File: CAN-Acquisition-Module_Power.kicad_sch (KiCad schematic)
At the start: 37 parts, among them J1 Conn_01x04, J2 Conn_01x02, Q1 SI2318A, U1 TL431DBZ, U2 S-8581AA

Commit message: Finished power outputs
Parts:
- L2: value 470 uF -> 470 uH
- U1: value TL431DBZ -> AZ431LAN
- renumbered C11 to C10, C12 to C11, C13 to C12, C14 to C13, C4 to C3, C5 to C4, C6 to C5, C7 to C6, C8 to C7, C9 to C8, C10 to C9
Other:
- note added: "1.24V"
- note added: "20ppm/°C or better"

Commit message: Only CAN transceiver left
SPi flash should be added too
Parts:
- added NT1: NetTie_2, CAN-Acquisition-Module:Net_Tie_small, symbol Device:NetTie_2
- C6: footprint Capacitor_THT:CP_Radial_D10.0mm_P5.00mm -> CAN-Acquisition-Module:CP_Radial_D10.0mm_P5.00mm_Horizontal
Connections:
- net at C6.1, C7.1, C8.1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: now also NT1.1; no longer U2.1 (VIN), U2.3 (EN)
- new net: NT1.2, U2.1 (VIN), U2.3 (EN)
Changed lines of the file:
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@@
     (stroke (width 0) (type default) (color 0 0 0 0))
   )
-  (wire (pts (xy 177.8 95.25) (xy 170.18 95.25))
+  (wire (pts (xy 177.8 95.25) (xy 176.53 95.25))
     (stroke (width 0) (type default) (color 0 0 0 0))
   )
@@
   )
   (wire (pts (xy 203.2 100.33) (xy 207.01 100.33))
+    (stroke (width 0) (type default) (color 0 0 0 0))
+  )
+  (wire (pts (xy 171.45 95.25) (xy 170.18 95.25))
     (stroke (width 0) (type default) (color 0 0 0 0))
   )
@@
       (effects (font (size 1.27 1.27)) (justify left))
     )
-    (property "Footprint" "Capacitor_THT:CP_Radial_D10.0mm_P5.00mm" (id 2) (at 140.97 119.38 90)
+    (property "Footprint" "CAN-Acquisition-Module:CP_Radial_D10.0mm_P5.00mm_Horizontal" (id 2) (at 140.97 119.38 90)
       (effects (font (size 1.27 1.27)) hide)
     )
@@
       (effects (font (size 1.27 1.27)) hide)
     )
+    (pin "1")
+    (pin "2")
+  )
+  (symbol (lib_id "Device:NetTie_2") (at 173.99 95.25 0) (unit 1)
+    (in_bom yes) (on_board yes) (fields_autoplaced)
+    (property "Reference" "NT1" (id 0) (at 173.99 91.5502 0))
+    (property "Value" "NetTie_2" (id 1) (at 173.99 94.0871 0))
+    (property "Footprint" "CAN-Acquisition-Module:Net_Tie_small" (id 2) (at 173.99 95.25 0)
+      (effects (font (size 1.27 1.27)) hide)
+    )
+    (property "Datasheet" "~" (id 3) (at 173.99 95.25 0)
+      (effects (font (size 1.27 1.27)) hide)
+    )

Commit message: forgor to save
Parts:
- added C13: 10 uF, Capacitor_SMD:C_0805_2012Metric, symbol Device:C_Small
- renumbered C13 to C14
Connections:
- net +3V3: now also C13.1
- net GND: now also C13.2
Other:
- moved on the sheet: C14

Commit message: Rev. A1 release
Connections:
- net at NT1.2, U2.1 (VIN), U2.3 (EN): now also C7.1, C8.1
- net at C6.1, L2.2, NT1.1: no longer C7.1, C8.1
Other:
- note added: "50V"
- note added: "50V rating"
- note added: "}"
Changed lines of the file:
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@@
-    (stroke (width 0) (type default) (color 0 0 0 0))
-  )
-  (wire (pts (xy 177.8 95.25) (xy 176.53 95.25))
     (stroke (width 0) (type default) (color 0 0 0 0))
   )
@@
     (stroke (width 0) (type default) (color 0 0 0 0))
   )
+  (wire (pts (xy 153.67 95.25) (xy 157.48 95.25))
+    (stroke (width 0) (type default) (color 0 0 0 0))
+  )
   (wire (pts (xy 157.48 95.25) (xy 157.48 100.33))
     (stroke (width 0) (type default) (color 0 0 0 0))
@@
     (stroke (width 0) (type default) (color 0 0 0 0))
   )
-  (wire (pts (xy 171.45 95.25) (xy 170.18 95.25))
+  (wire (pts (xy 170.18 95.25) (xy 177.8 95.25))
     (stroke (width 0) (type default) (color 0 0 0 0))
   )
@@
     (stroke (width 0) (type default) (color 0 0 0 0))
   )
-  (wire (pts (xy 144.78 95.25) (xy 157.48 95.25))
+  (wire (pts (xy 144.78 95.25) (xy 148.59 95.25))
     (stroke (width 0) (type default) (color 0 0 0 0))
   )
@@
     (stroke (width 0) (type default) (color 0 0 0 0))
   )
-  (text "5 to 24V" (at 152.4 95.25 0)
+  (text "}" (at 170.18 95.25 90)
+    (effects (font (size 20 20)) (justify left bottom))
+  )
+  (text "50V" (at 114.3 106.68 0)
+    (effects (font (size 1.27 1.27)) (justify left bottom))
+  )
+  (text "5 to 24V" (at 153.67 95.25 0)
     (effects (font (size 1.27 1.27)) (justify left bottom))
   )
@@
   )
   (text "1.24V" (at 60.96 170.18 0)
+    (effects (font (size 1.27 1.27)) (justify left bottom))
+  )
+  (text "50V rating" (at 153.67 85.09 0)
     (effects (font (size 1.27 1.27)) (justify left bottom))
   )
@@
       (effects (font (size 1.27 1.27)) hide)
     )
-    (property "P/N" "GRM31CR71H475KA12L" (id 7) (at 153.67 118.11 90))
+    (property "P/N" "GRM31CR71H475KA12L" (id 7) (at 153.67 115.57 90))
     (property "Rated Voltage" "50V" (id 8) (at 157.48 102.87 0)
       (effects (font (size 1.27 1.27)) hide)
@@
     (pin "2")
   )
-  (symbol (lib_id "Device:NetTie_2") (at 173.99 95.25 0) (unit 1)
-    (in_bom yes) (on_board yes) (fields_autoplaced)
-    (property "Reference" "NT1" (id 0) (at 173.99 91.5502 0))
-    (property "Value" "NetTie_2" (id 1) (at 173.99 94.0871 0))
-    (property "Footprint" "CAN-Acquisition-Module:Net_Tie_small" (id 2) (at 173.99 95.25 0)
-      (effects (font (size 1.27 1.27)) hide)
-    )
-    (property "Datasheet" "~" (id 3) (at 173.99 95.25 0)
-      (effects (font (size 1.27 1.27)) hide)
-    )
+  (symbol (lib_id "Device:NetTie_2") (at 151.13 95.25 0) (unit 1)
+    (in_bom yes) (on_board yes) (fields_autoplaced)
+    (property "Reference" "NT1" (id 0) (at 151.13 91.5502 0)
+      (effects (font (size 1.27 1.27)) hide)
+    )
+    (property "Value" "NetTie_2" (id 1) (at 151.13 94.0871 0)
+      (effects (font (size 1.27 1.27)) hide)
+    )
+    (property "Footprint" "CAN-Acquisition-Module:Net_Tie_small" (id 2) (at 151.13 95.25 0)
+      (effects (font (size 1.27 1.27)) hide)
+    )
+    (property "Datasheet" "~" (id 3) (at 151.13 95.25 0)
+      (effects (font (size 1.27 1.27)) hide)
+    )

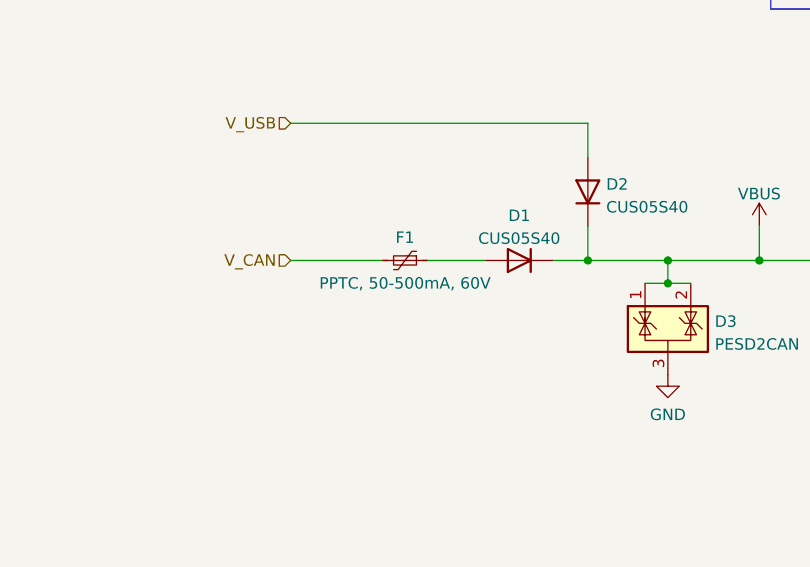
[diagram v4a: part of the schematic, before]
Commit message: Added as-ordered P/Ns and regenerated Gerbers
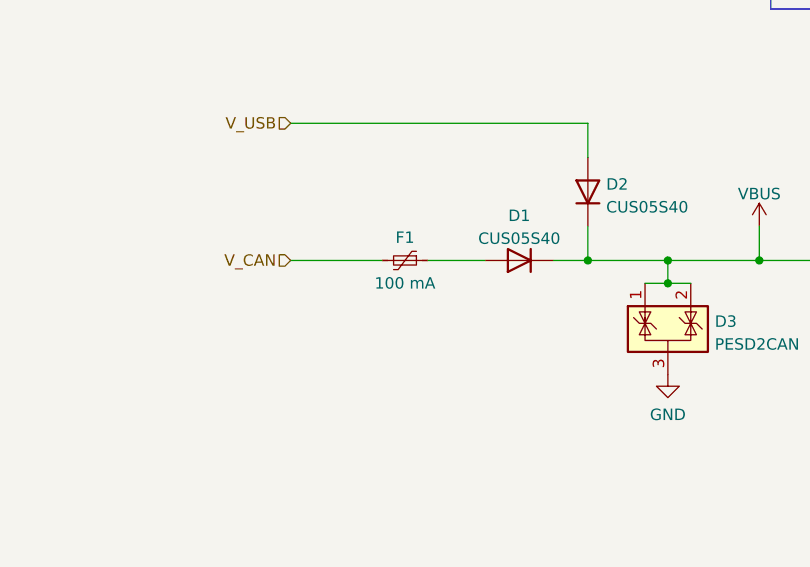
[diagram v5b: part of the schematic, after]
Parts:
- C11: Mfr. (none) -> Kemet; P/N (none) -> C0603C330J1GACAUTO
- D1, D2, D6: P/N (none) -> CUS05S40,H3F
- D3: Mfr. (none) -> Comchip Technology; P/N (none) -> CPDT-24V
- D4, D5: Mfr. (none) -> Diodes Incorporated; P/N (none) -> D1213A-01SO-7
- F1: value PPTC, 50-500mA, 60V -> 100 mA
- L1: Mfr. (none) -> Eaton; P/N (none) -> MFBM1V1608-300-R
- L2: Mfr. (none) -> Murata Electronics
- Q1: Mfr. (none) -> Micro Commercial Co.; P/N (none) -> SI2318A-TP
- R1: Mfr. (none) -> Stackpole; P/N (none) -> RNCP0805FTD100R
- R2: Mfr. (none) -> Panasonic; P/N (none) -> ERJ-PB3B6801V
- R3, R9: Mfr. (none) -> KOA Speer; P/N (none) -> RN73R1JTTD1502B25
- R5, R6, R7: Mfr. (none) -> Stackpole; P/N (none) -> RMCF0603FT10K0
- R8: Mfr. (none) -> TE Connectivity; P/N (none) -> CRGCQ0603F47K
- U1: Mfr. (none) -> Diodes Incorporated; P/N (none) -> AZ431LANTR-G1
- U2: Mfr. (none) -> Ablic; P/N (none) -> S-8581AA-A8T1U7
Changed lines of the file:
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@@
       (effects (font (size 1.27 1.27) italic) hide)
     )
+    (property "Mfr." "Diodes Incorporated" (id 4) (at 67.31 170.18 0)
+      (effects (font (size 1.27 1.27)) hide)
+    )
+    (property "P/N" "AZ431LANTR-G1" (id 5) (at 67.31 170.18 0)
+      (effects (font (size 1.27 1.27)) hide)
+    )
     (pin "1")
     (pin "2")
@@
       (effects (font (size 1.27 1.27)) hide)
     )
+    (property "Mfr." "Panasonic" (id 4) (at 57.15 166.37 0)
+      (effects (font (size 1.27 1.27)) hide)
+    )
+    (property "P/N" "ERJ-PB3B6801V" (id 5) (at 57.15 166.37 0)
+      (effects (font (size 1.27 1.27)) hide)
+    )
     (pin "1")
     (pin "2")
@@
     )
     (property "Datasheet" "~" (id 3) (at 57.15 173.99 0)
+      (effects (font (size 1.27 1.27)) hide)
+    )
+    (property "Mfr." "KOA Speer" (id 4) (at 57.15 173.99 0)
+      (effects (font (size 1.27 1.27)) hide)
+    )
+    (property "P/N" "RN73R1JTTD1502B25" (id 5) (at 57.15 173.99 0)
       (effects (font (size 1.27 1.27)) hide)
     )
@@
       (effects (font (size 1.27 1.27)) hide)
     )
+    (property "Mfr." "Stackpole" (id 4) (at 49.53 161.29 0)
+      (effects (font (size 1.27 1.27)) hide)
+    )
+    (property "P/N" "RNCP0805FTD100R" (id 5) (at 49.53 161.29 0)
+      (effects (font (size 1.27 1.27)) hide)
+    )
     (pin "1")
     (pin "2")
@@
       (effects (font (size 1.27 1.27)) hide)
     )
+    (property "Mfr." "Eaton" (id 4) (at 39.37 161.29 0)
+      (effects (font (size 1.27 1.27)) hide)
+    )
+    (property "P/N" "MFBM1V1608-300-R" (id 5) (at 39.37 161.29 0)
+      (effects (font (size 1.27 1.27)) hide)
+    )
     (pin "1")
     (pin "2")
@@
       (effects (font (size 1.27 1.27)) hide)
     )
+    (property "P/N" "CUS05S40,H3F" (id 5) (at 238.76 34.29 0)
+      (effects (font (size 1.27 1.27)) hide)
+    )
     (pin "1")
     (pin "2")
@@
     )
     (property "Datasheet" "https://assets.nexperia.com/documents/data-sheet/PESD2CAN.pdf" (id 3) (at 94.615 99.695 0)
+      (effects (font (size 1.27 1.27)) hide)
+    )
+    (property "Mfr." "Comchip Technology" (id 4) (at 91.44 102.87 0)
+      (effects (font (size 1.27 1.27)) hide)
+    )
+    (property "P/N" "CPDT-24V" (id 5) (at 91.44 102.87 0)
       (effects (font (size 1.27 1.27)) hide)
     )
@@
     )
     (property "Datasheet" "https://www.ablic.com/en/doc/datasheet/switching_regulator/S8580AA_8580AB_8581AA_8581AB_E.pdf" (id 3) (at 201.93 120.65 0)
+      (effects (font (size 1.27 1.27)) hide)
+    )
+    (property "Mfr." "Ablic" (id 4) (at 187.96 92.71 0)
+      (effects (font (size 1.27 1.27)) hide)
+    )
+    (property "P/N" "S-8581AA-A8T1U7" (id 5) (at 187.96 92.71 0)
       (effects (font (size 1.27 1.27)) hide)
     )
@@
       (effects (font (size 1.27 1.27)) hide)
     )
+    (property "Mfr." "Stackpole" (id 4) (at 173.99 44.45 0)
+      (effects (font (size 1.27 1.27)) hide)
+    )
+    (property "P/N" "RMCF0603FT10K0" (id 5) (at 173.99 44.45 0)
+      (effects (font (size 1.27 1.27)) hide)
+    )
     (pin "1")
     (pin "2")
@@
       (effects (font (size 1.27 1.27)) hide)
     )
+    (property "Mfr." "Murata Electronics" (id 5) (at 124.46 95.25 0)
+      (effects (font (size 1.27 1.27)) hide)
+    )
     (pin "1")
     (pin "2")
@@
       (effects (font (size 1.27 1.27)) hide)
     )
+    (property "Mfr." "Diodes Incorporated" (id 4) (at 168.91 26.67 0)
+      (effects (font (size 1.27 1.27)) hide)
+    )
+    (property "P/N" "D1213A-01SO-7" (id 5) (at 168.91 26.67 0)
+      (effects (font (size 1.27 1.27)) hide)
+    )
     (pin "1")
     (pin "2")
@@
       (effects (font (size 1.27 1.27)) hide)
     )
+    (property "Mfr." "Stackpole" (id 4) (at 227.33 53.34 0)
+      (effects (font (size 1.27 1.27)) hide)
+    )
+    (property "P/N" "RMCF0603FT10K0" (id 5) (at 227.33 53.34 0)
+      (effects (font (size 1.27 1.27)) hide)
+    )
     (pin "1")
     (pin "2")
@@
       (effects (font (size 1.27 1.27)) hide)
     )
+    (property "P/N" "CUS05S40,H3F" (id 5) (at 82.55 87.63 0)
+      (effects (font (size 1.27 1.27)) hide)
+    )
     (pin "1")
     (pin "2")
@@
       (effects (font (size 1.27 1.27)) hide)
     )
+    (property "Mfr." "Diodes Incorporated" (id 4) (at 146.05 26.67 0)
+      (effects (font (size 1.27 1.27)) hide)
+    )
+    (property "P/N" "D1213A-01SO-7" (id 5) (at 146.05 26.67 0)
+      (effects (font (size 1.27 1.27)) hide)
+    )
     (pin "1")
     (pin "2")
@@
       (effects (font (size 1.27 1.27)) hide)
     )
+    (property "Mfr." "KOA Speer" (id 4) (at 232.41 105.41 0)
+      (effects (font (size 1.27 1.27)) hide)
+    )
+    (property "P/N" "RN73R1JTTD1502B25" (id 5) (at 232.41 105.41 0)
+      (effects (font (size 1.27 1.27)) hide)
+    )
     (pin "1")
     (pin "2")
@@
     )
     (property "Datasheet" "~" (id 3) (at 223.52 99.06 0)
+      (effects (font (size 1.27 1.27)) hide)
+    )
+    (property "Mfr." "Kemet" (id 4) (at 223.52 99.06 0)
+      (effects (font (size 1.27 1.27)) hide)
+    )
+    (property "P/N" "C0603C330J1GACAUTO" (id 5) (at 223.52 99.06 0)
       (effects (font (size 1.27 1.27)) hide)
     )
@@
       (effects (font (size 1.27 1.27)) hide)
     )
+    (property "P/N" "CUS05S40,H3F" (id 5) (at 74.93 95.25 0)
+      (effects (font (size 1.27 1.27)) hide)
+    )
     (pin "1")
     (pin "2")
@@
       (effects (font (size 1.27 1.27)) hide)
     )
+    (property "Mfr." "Stackpole" (id 4) (at 180.34 46.99 0)
+      (effects (font (size 1.27 1.27)) hide)
+    )
+    (property "P/N" "RMCF0603FT10K0" (id 5) (at 180.34 46.99 0)
+      (effects (font (size 1.27 1.27)) hide)
+    )
     (pin "1")
     (pin "2")
@@
       (effects (font (size 1 1)) hide)
     )
+    (property "Mfr." "Micro Commercial Co." (id 5) (at 236.22 53.34 0)
+      (effects (font (size 1.27 1.27)) hide)
+    )
+    (property "P/N" "SI2318A-TP" (id 6) (at 236.22 53.34 0)
+      (effects (font (size 1.27 1.27)) hide)
+    )
     (pin "1")
     (pin "2")
@@
       (effects (font (size 1.27 1.27)) hide)
     )
+    (property "Mfr." "TE Connectivity" (id 4) (at 232.41 99.06 0)
+      (effects (font (size 1.27 1.27)) hide)
+    )
+    (property "P/N" "CRGCQ0603F47K" (id 5) (at 232.41 99.06 0)
+      (effects (font (size 1.27 1.27)) hide)
+    )
     (pin "1")
     (pin "2")
@@
     (in_bom yes) (on_board yes)
     (property "Reference" "F1" (id 0) (at 62.23 92.71 90))
-    (property "Value" "PPTC, 50-500mA, 60V" (id 1) (at 62.23 97.79 90))
+    (property "Value" "100 mA" (id 1) (at 62.23 97.79 90))
     (property "Footprint" "Fuse:Fuse_1206_3216Metric" (id 2) (at 57.15 96.52 0)
       (effects (font (size 1.27 1.27)) (justify left) hide)

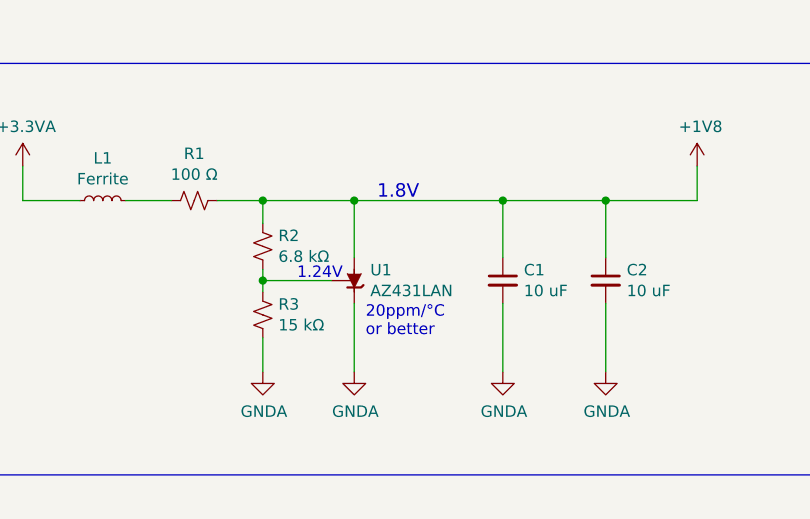
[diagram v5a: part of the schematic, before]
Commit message: Rev. A2
U1 had wrong pinout. NT1 label removed from silk. Green LED resistor increased in value
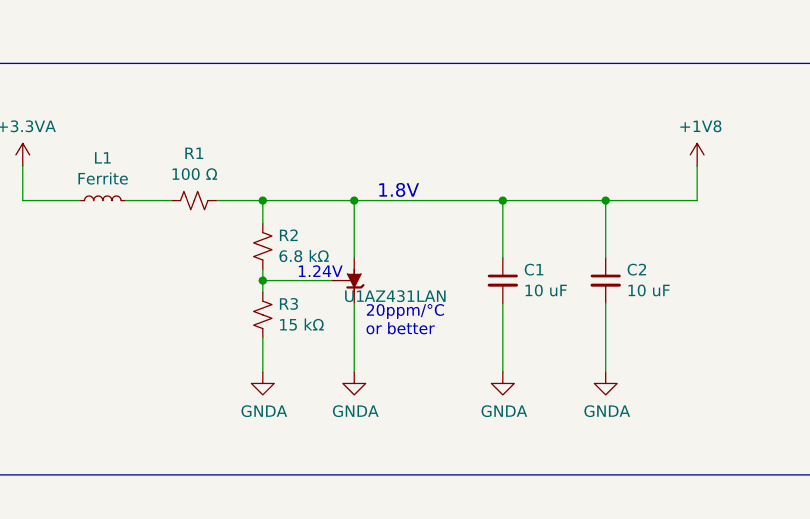
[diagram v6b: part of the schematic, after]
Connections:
- net GNDA: now also U1.2 (K); no longer U1.1 (K)
- net at R2.2, R3.1: now also U1.1 (REF); no longer U1.2 (REF)
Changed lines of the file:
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@@
   (symbol (lib_id "Reference_Voltage:TL431DBZ") (at 67.31 170.18 90) (mirror x) (unit 1)
     (in_bom yes) (on_board yes)
-    (property "Reference" "U1" (id 0) (at 69.088 169.0116 90)
+    (property "Reference" "U1" (id 0) (at 66.1416 171.958 90)
       (effects (font (size 1.27 1.27)) (justify right))
     )
-    (property "Value" "AZ431LAN" (id 1) (at 69.088 171.323 90)
+    (property "Value" "AZ431LAN" (id 1) (at 68.453 171.958 90)
       (effects (font (size 1.27 1.27)) (justify right))
     )
-    (property "Footprint" "Package_TO_SOT_SMD:SOT-23" (id 2) (at 71.12 170.18 0)
+    (property "Footprint" "Package_TO_SOT_SMD:SOT-23" (id 2) (at 69.85 173.99 0)
       (effects (font (size 1.27 1.27) italic) hide)
     )
-    (property "Datasheet" "http://www.ti.com/lit/ds/symlink/tl431.pdf" (id 3) (at 67.31 170.18 0)
+    (property "Datasheet" "http://www.ti.com/lit/ds/symlink/tl431.pdf" (id 3) (at 71.12 170.18 0)
       (effects (font (size 1.27 1.27) italic) hide)
     )
-    (property "Mfr." "Diodes Incorporated" (id 4) (at 67.31 170.18 0)
+    (property "Mfr." "Diodes Incorporated" (id 4) (at 72.39 170.18 0)
       (effects (font (size 1.27 1.27)) hide)
     )
-    (property "P/N" "AZ431LANTR-G1" (id 5) (at 67.31 170.18 0)
+    (property "P/N" "AZ431LANTR-G1" (id 5) (at 73.66 170.18 0)
       (effects (font (size 1.27 1.27)) hide)
     )
+    (pin "2")
     (pin "1")
-    (pin "2")
     (pin "3")
   )
